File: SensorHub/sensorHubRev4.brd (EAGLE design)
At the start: 80 x 80 mm, 57 parts, among them IC1 ADP3338AKCZ-3.3, IC2 FT231XQ, U2 TPS2065DBVR, U3 BS138PS, X1 32.768k, X2 332-02, X3 332-02

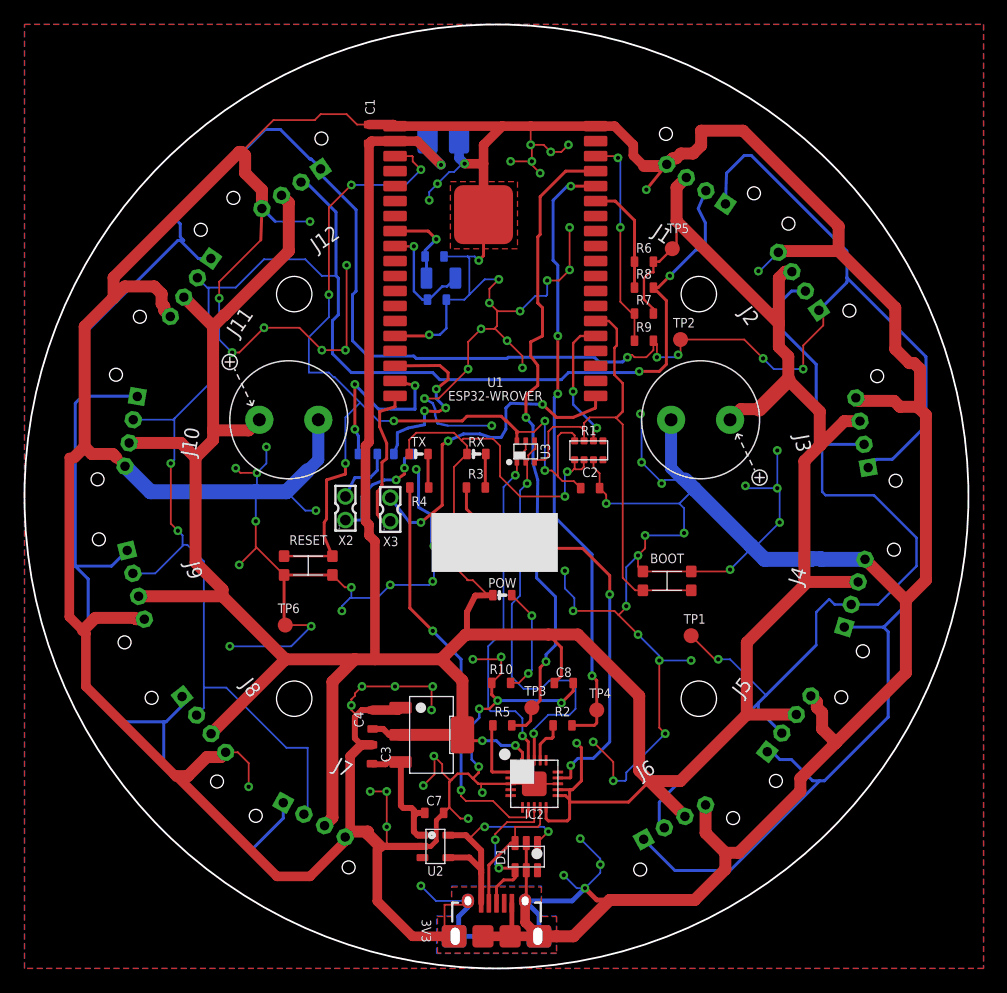
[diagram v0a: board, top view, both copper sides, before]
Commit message: SensorHubRev4Update
Addtion i2C EMI Filter Add
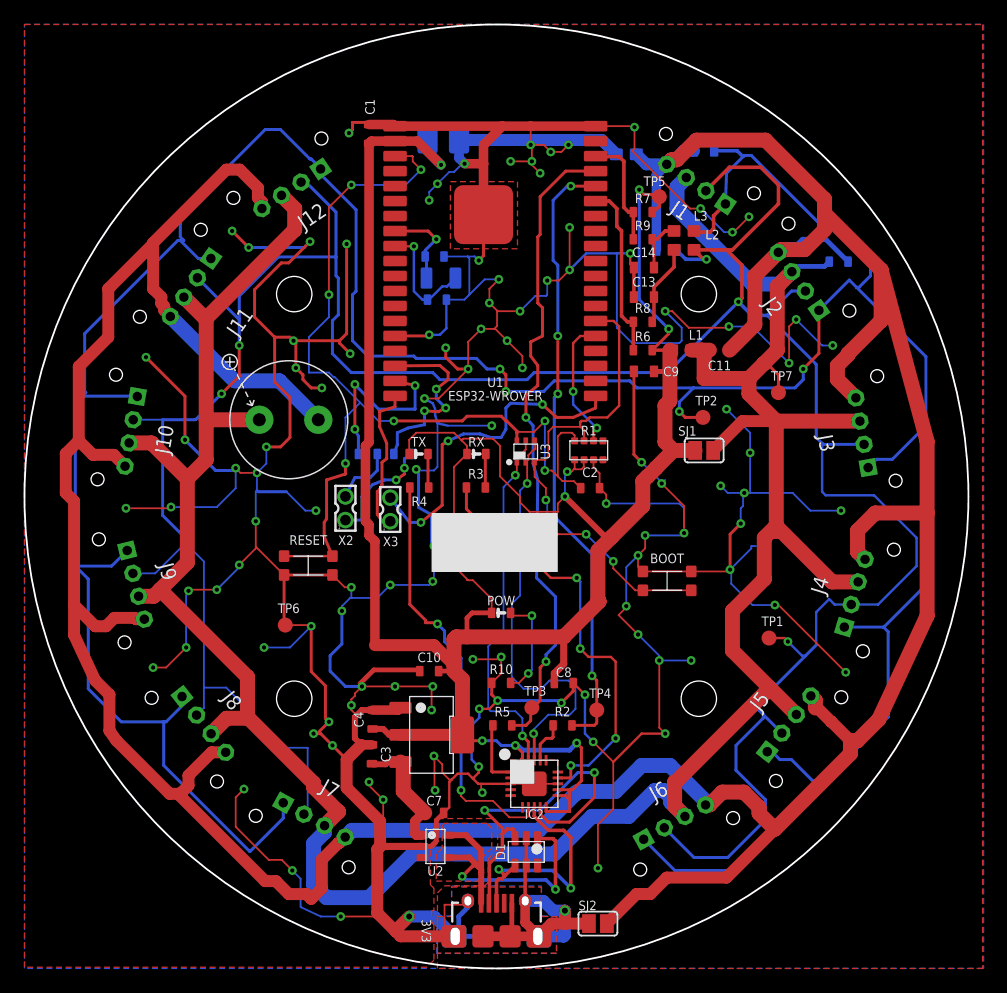
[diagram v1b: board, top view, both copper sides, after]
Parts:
- removed U$3: RUBYCONWXA1000UF/10V, FaBo-Capacitor:ALUMINUM10*9
- added C10: DNP, component:EIA0603
- added C11, C9: 10uF, FaBo-Capacitor:0603-NARROW
- added C13, C14, C15, C16: 33pF, FaBo-Capacitor:0603-NARROW
- added C17: 0.1uF, component:EIA0603
- added L1, L2, L3, L4: BLM18EG221SN1, FaBo-Inductor:0603
- added SJ1, SJ2: (no value), jumper:SJ
- added TP7: TPB1,27, testpad:B1,27
- C4: value 1uF -> 2.2uF
- R8, R9: value 1k -> 22
- moved R7 8.60 mm to (52.4, 64.1)
- moved R9 8.60 mm to (52.4, 61.8)
- moved R6 7.50 mm to (52.4, 52.4)
- moved TP2 6.87 mm to (57.5, 46.7)
- moved TP1 6.60 mm to (63.1, 28.0)
- moved TP5 4.54 mm to (53.8, 65.4)
- moved R8 2.90 mm to (52.4, 54.8)
- moved POW 1.50 mm to (40.4, 30.1)
- moved D1 0.40 mm to (42.5, 9.88)
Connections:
- new net GNDIO: C11.1, C15.1, C16.1, C17.1, J1.GND, J10.GND, J11.GND, J12.GND, J2.GND, J3.GND, J4.GND, J5.GND, J6.GND, J7.GND, J8.GND, J9.GND, L4.2, SJ2.2, U$2.MINUS
- new net N$7: C13.2, L2.1, R8.2
- new net N$8: C14.2, L3.1, R9.2
- new net VCCIO: C11.2, C17.2, J1.VCC, J10.VCC, J11.VCC, J12.VCC, J2.VCC, J3.VCC, J4.VCC, J5.VCC, J6.VCC, J7.VCC, J8.VCC, J9.VCC, L1.2, SJ1.1, TP7.TP, U$2.PLUS
- net 3V3: now also C10.2, C9.2, L1.1, SJ1.2; no longer J1.VCC, J10.VCC, J11.VCC, J12.VCC, J2.VCC, J3.VCC, J4.VCC, J5.VCC, J6.VCC, J7.VCC, J8.VCC, J9.VCC, U$2.PLUS, U$3.PLUS
- net GND: now also C10.1, C13.1, C14.1, C9.1, L4.1, SJ2.1; no longer J1.GND, J10.GND, J11.GND, J12.GND, J2.GND, J3.GND, J4.GND, J5.GND, J6.GND, J7.GND, J8.GND, J9.GND, U$2.MINUS, U$3.MINUS
- net SCL: now also C16.2, L3.2; no longer R9.2
- net SDA: now also C15.2, L2.2; no longer R8.2
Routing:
- net GNDIO: track 0.00 -> 331.4 mm
- net VCCIO: track 0.00 -> 238.3 mm
- net 3V3: track 378.6 -> 219.3 mm, vias 6 -> 8
- net GND: track 769.7 -> 678.1 mm, vias 92 -> 113
- net SDA: track 233.0 -> 252.4 mm
- net USBDM: track 11.3 -> 29.9 mm, vias 0 -> 2
- net SCL: track 277.1 -> 289.9 mm, vias 5 -> 4
- net N$6: track 18.2 -> 9.95 mm, vias 2 -> 0
- net USBVBUS: track 19.9 -> 27.0 mm
- net USBDP: track 13.4 -> 20.4 mm
- net N$7: track 0.00 -> 6.87 mm
- net N$5: track 9.67 -> 15.0 mm
- net N$8: track 0.00 -> 4.60 mm
- net IO0: track 41.5 -> 42.6 mm, vias 0 -> 4
- net LED1K: track 9.30 -> 8.76 mm
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- added copper zone on layer 1, net USBVBUS
